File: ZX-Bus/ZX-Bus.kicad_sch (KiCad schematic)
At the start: 40 parts, among them J1 DIP-40 Pins, J2 Conn_01x04_Pin, J3 Conn_01x08_Pin, J4 Power, J5 Main board power, J6 12V, J7 5V, J8 Reset, U1 Z84C00xxP, U2 74LS245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

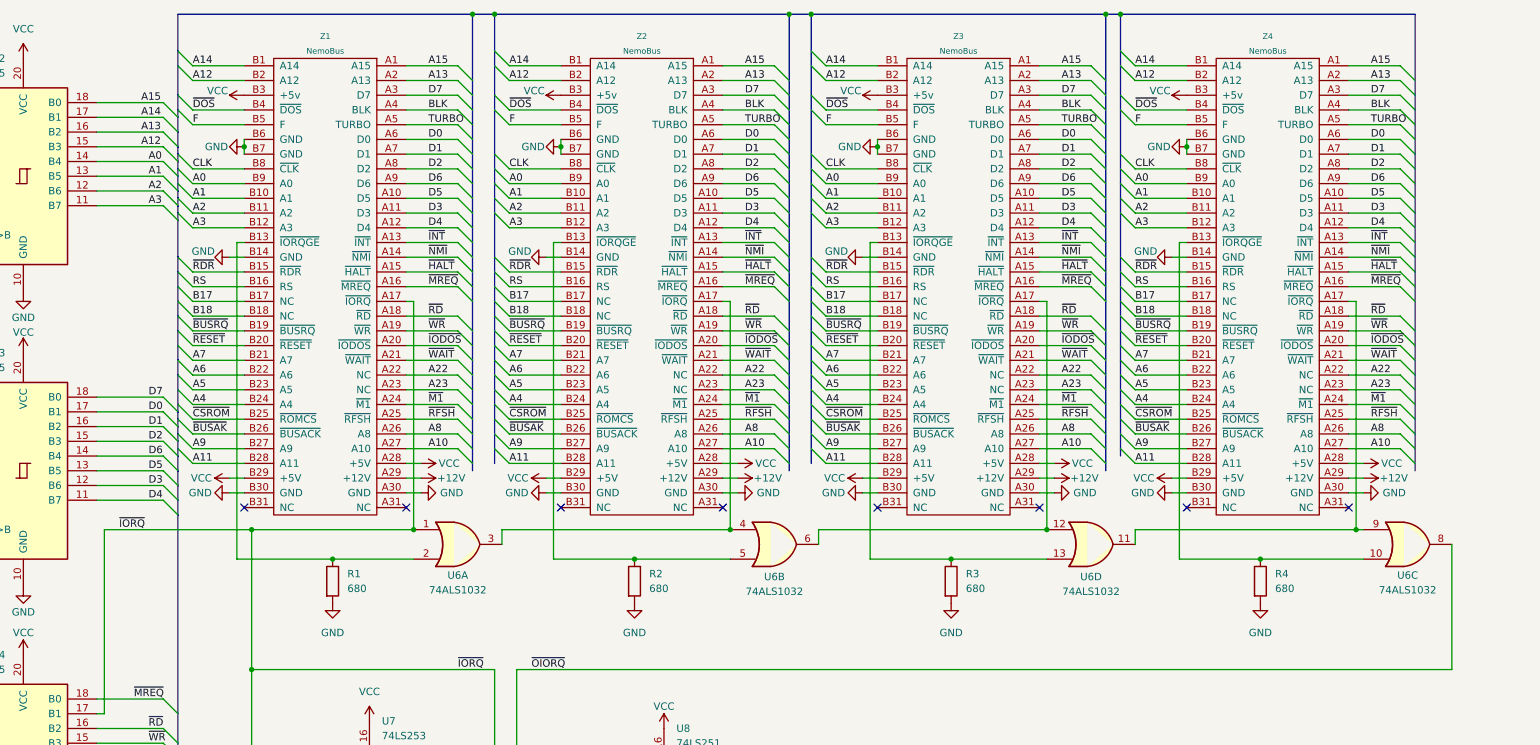
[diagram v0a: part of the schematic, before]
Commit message: ZX-Bus: Flip slots on the schematic
This is actually original orientation, during schematic creation i flipped them
for historical reason. It's easier to compare with other versions.
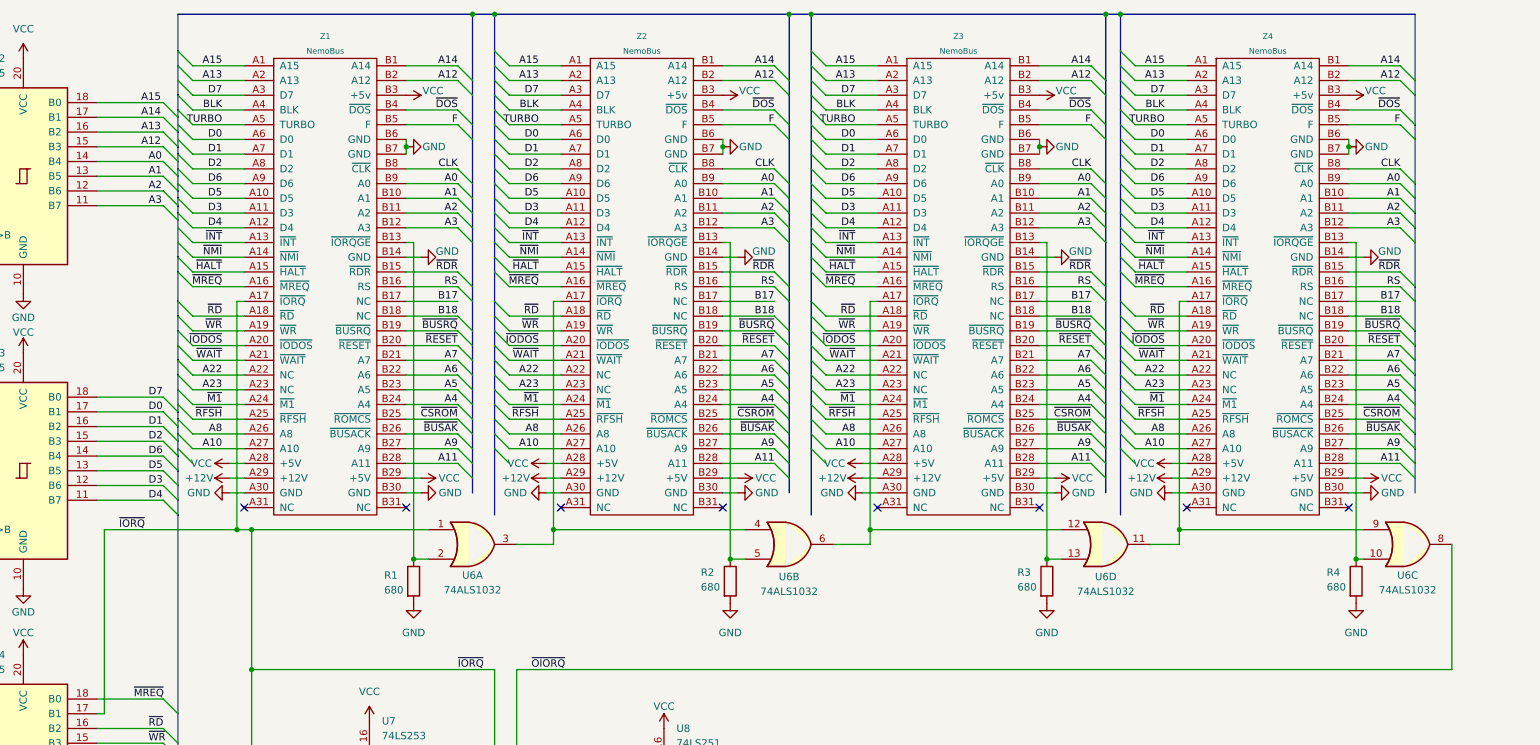
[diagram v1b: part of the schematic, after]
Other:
- moved on the sheet: R1, R2, R3, R4, U6A, U6B, U6D

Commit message: ZX-Bus: Complete v1
Add missing parts and complete layout
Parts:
- removed C12, C13: 220uF, Capacitor_THT:CP_Radial_D5.0mm_P2.50mm, symbol Device:C_Polarized
- removed J2: Conn_01x04_Pin, Connector_PinHeader_2.54mm:PinHeader_1x04_P2.54mm_Vertical, symbol Connector:Conn_01x04_Pin
- removed J3: Conn_01x08_Pin, Connector_PinHeader_2.54mm:PinHeader_1x08_P2.54mm_Vertical, symbol Connector:Conn_01x08_Pin
- added C12, C13, C14: 0.1uF, Capacitor_THT:C_Disc_D4.3mm_W1.9mm_P5.00mm, symbol Device:C
- added C15, C16: 220uF, Capacitor_THT:CP_Radial_D5.0mm_P2.50mm, symbol Device:C_Polarized
- added H3: MountingHole 3mm, MountingHole:MountingHole_3mm_Pad, symbol Mechanical:MountingHole_Pad
- added J2: PLS-3, Connector_PinHeader_2.54mm:PinHeader_1x03_P2.54mm_Vertical, symbol Connector:Conn_01x03_Pin
- added J3: PLS-6, Connector_PinHeader_2.54mm:PinHeader_1x05_P2.54mm_Vertical, symbol Connector:Conn_01x05_Pin
- added J9: PLS-2R, Connector_PinHeader_2.54mm:PinHeader_1x02_P2.54mm_Horizontal, symbol Connector:Conn_01x02_Pin
- added JP2: ROM type, Connector_PinHeader_2.54mm:PinHeader_1x03_P2.54mm_Vertical, symbol Jumper:Jumper_3_Bridged12
- added R5: 510, Resistor_THT:R_Axial_DIN0207_L6.3mm_D2.5mm_P10.16mm_Horizontal, symbol Device:R
- added R6: 10K, Resistor_THT:R_Axial_DIN0204_L3.6mm_D1.6mm_P2.54mm_Vertical, symbol Device:R
- added U10, U9: 27128, Package_DIP:DIP-28_W15.24mm_Socket, symbol Memory_EPROM:27128
- added U11: 74ALS1032, Package_DIP:DIP-14_W7.62mm, symbol 74xx:74LS32
- J8: footprint Connector_PinHeader_2.54mm:PinHeader_1x02_P2.54mm_Horizontal -> Connector_PinHeader_2.54mm:PinHeader_1x02_P2.54mm_Vertical
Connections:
- net *A0: now also U10.10 (A0), U9.10 (A0)
- net *A1: now also U10.9 (A1), U9.9 (A1)
- net *A10: now also U10.21 (A10), U9.21 (A10)
- net *A11: now also U10.23 (A11), U9.23 (A11)
- net *A12: now also U10.2 (A12), U9.2 (A12)
- net *A13: now also U10.26 (A13), U9.26 (A13)
- net *A14: now also U11.2
- net *A15: now also U11.1
- net *A2: now also U10.8 (A2), U9.8 (A2)
- net *A3: now also U10.7 (A3), U9.7 (A3)
- net *A4: now also U10.6 (A4), U9.6 (A4)
- net *A5: now also U10.5 (A5), U9.5 (A5)
- net *A6: now also U10.4 (A6), U9.4 (A6)
- net *A7: now also U10.3 (A7), U9.3 (A7)
- net *A8: now also U10.25 (A8), U9.25 (A8)
- net *A9: now also U10.24 (A9), U9.24 (A9)
- net *D0: now also U10.11 (D0), U9.11 (D0)
- net *D1: now also U10.12 (D1), U9.12 (D1)
- net *D2: now also U10.13 (D2), U9.13 (D2)
- net *D3: now also U10.15 (D3), U9.15 (D3)
- net *D4: now also U10.16 (D4), U9.16 (D4)
- net *D5: now also U10.17 (D5), U9.17 (D5)
- net *D6: now also U10.18 (D6), U9.18 (D6)
- net *D7: now also U10.19 (D7), U9.19 (D7)
- net *~{MREQ}: now also U11.4
- net *~{RD}: now also U11.5
- net +12V: now also C16.1
- net A22: now also J3.4 (Pin_4)
- net A23: now also J3.5 (Pin_5)
- net B17: now also J3.1 (Pin_1)
- net B18: now also J3.2 (Pin_2)
- net BLK: now also J2.1 (Pin_1)
- net F: now also J2.3 (Pin_3)
- net GND: now also C12.2, C13.2, C14.2, C15.2, C16.2, H3.1, U10.14 (GND), U11.12, U11.13, U11.7 (GND), U9.14 (GND)
- net RS: now also R6.1
- net TURBO: now also J2.2 (Pin_2)
- net VCC: now also C12.1, C13.1, C14.1, C15.1, JP2.1 (A), R6.2, U10.1 (VPP), U10.27 (~{PGM}), U10.28 (VCC), U11.14 (VCC), U9.1 (VPP), U9.28 (VCC)
- net ~{CSROM}: now also R5.2, U11.8
- net ~{DOS}: now also J9.1 (Pin_1), JP2.3 (B), U10.22 (~{OE})
- net ~{RDR}: now also R5.1, U10.20 (~{CE}), U9.20 (~{CE})
- net ~{IODOS} renamed A20
- net A20: now also J3.3 (Pin_3)
- new net: U11.10, U11.3
- new net: U11.6, U11.9
- new net: JP2.2 (C), U9.27 (~{PGM})
- new net DOS: J9.2 (Pin_2), U9.22 (~{OE})
- no-connect marks 15 -> 16
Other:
- title: (none) -> NemoBus for Pentagon-48
- moved on the sheet: C1, C10, C11, C2, C3, C4, C5, C6, C8, C9, H1, H2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

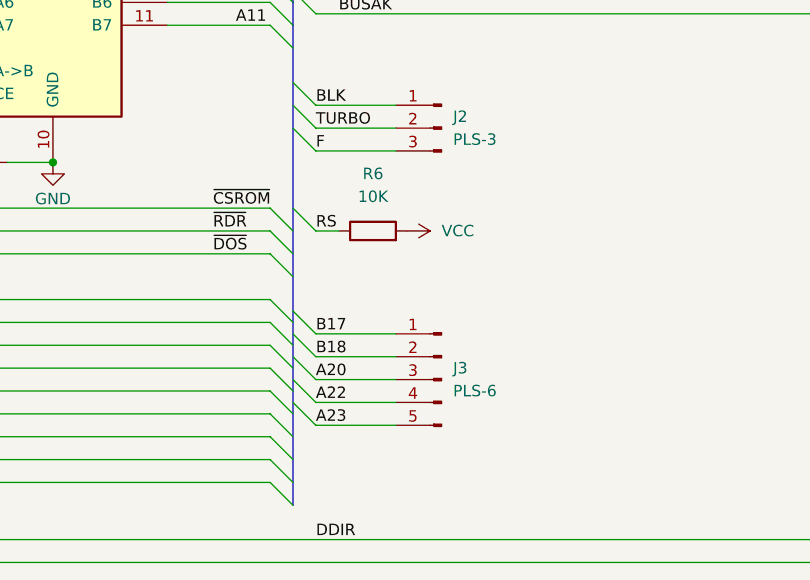
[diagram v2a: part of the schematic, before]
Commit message: ZX-Bus: Some corrections
Corrected size and layout after verification. SL-62 footprints with proper
courtyards.
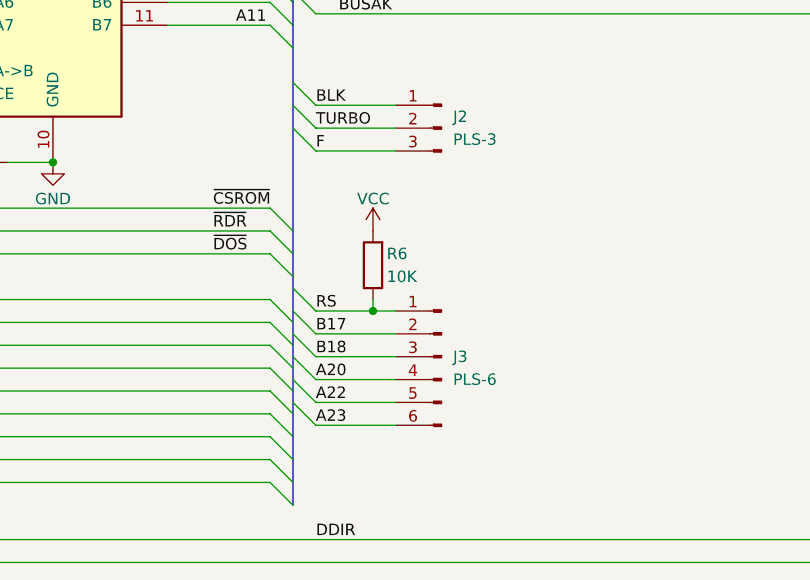
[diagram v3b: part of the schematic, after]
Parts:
- removed J3: PLS-6, Connector_PinHeader_2.54mm:PinHeader_1x05_P2.54mm_Vertical, symbol Connector:Conn_01x05_Pin
- added J3: PLS-6, Connector_PinHeader_2.54mm:PinHeader_1x06_P2.54mm_Vertical, symbol Connector:Conn_01x06_Pin
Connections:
- net A20: now also J3.4 (Pin_4)
- net A22: now also J3.5 (Pin_5)
- net A23: now also J3.6 (Pin_6)
- net B17: now also J3.2 (Pin_2)
- net B18: now also J3.3 (Pin_3)
- net RS: now also J3.1 (Pin_1)
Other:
- moved on the sheet: R6
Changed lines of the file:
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@@
 	)
 	(junction
+		(at 189.23 254)
+		(diameter 0)
+		(color 0 0 0 0)
+	)
+	(junction
 		(at 353.06 124.46)
 		(diameter 0)
@@
 	)
 	(bus_entry
+		(at 180.34 251.46)
+		(size 2.54 2.54)
+		(stroke
+			(width 0)
+			(type default)
+		)
+	)
+	(bus_entry
 		(at 234.95 105.41)
 		(size 2.54 2.54)
@@
 	)
 	(bus_entry
-		(at 180.34 242.57)
-		(size 2.54 2.54)
-		(stroke
-			(width 0)
-			(type default)
-		)
-	)
-	(bus_entry
 		(at 177.8 255.27)
 		(size 2.54 2.54)
@@
 	(wire
 		(pts
-			(xy 182.88 245.11) (xy 185.42 245.11)
-		)
-		(stroke
-			(width 0)
-			(type default)
-		)
-	)
-	(wire
-		(pts
 			(xy 166.37 58.42) (xy 177.8 58.42)
 		)
@@
 		)
 	)
+	(wire
+		(pts
+			(xy 189.23 254) (xy 189.23 252.73)
+		)
+		(stroke
+			(width 0)
+			(type default)
+		)
+	)
 	(bus
 		(pts
@@
 	(wire
 		(pts
+			(xy 182.88 254) (xy 189.23 254)
+		)
+		(stroke
+			(width 0)
+			(type default)
+		)
+	)
+	(wire
+		(pts
 			(xy 85.09 110.49) (xy 93.98 110.49)
 		)
@@
 		)
 	)
+	(wire
+		(pts
+			(xy 189.23 254) (xy 191.77 254)
+		)
+		(stroke
+			(width 0)
+			(type default)
+		)
+	)
 	(bus
 		(pts
@@
 		)
 	)
+	(label "RS"
+		(at 182.88 254 0)
+		(effects
+			(font
+				(size 1.27 1.27)
+			)
+			(justify left bottom)
+		)
+	)
 	(label "*A8"
 		(at 129.54 214.63 0)
@@
 		)
 	)
-	(label "RS"
-		(at 182.88 245.11 0)
-		(effects
-			(font
-				(size 1.27 1.27)
-			)
-			(justify left bottom)
-		)
-	)
 	(label "*D7"
 		(at 129.54 101.6 0)
@@
 	)
 	(symbol
-		(lib_id "Connector:Conn_01x05_Pin")
-		(at 196.85 261.62 0)
-		(mirror y)
-		(unit 1)
-		(body_style 1)
-		(exclude_from_sim no)
-		(in_bom yes)
-		(on_board yes)
-		(in_pos_files yes)
-		(dnp no)
-		(fields_autoplaced yes)
-		(property "Reference" "J3"
-			(at 198.12 260.3499 0)
-			(show_name no)
-			(do_not_autoplace no)
-			(effects
-				(font
-					(size 1.27 1.27)
-				)
-				(justify right)
-			)
-		)
-		(property "Value" "PLS-6"
-			(at 198.12 262.8899 0)
-			(show_name no)
-			(do_not_autoplace no)
-			(effects
-				(font
-					(size 1.27 1.27)
-				)
-				(justify right)
-			)
-		)
-		(property "Footprint" "Connector_PinHeader_2.54mm:PinHeader_1x05_P2.54mm_Vertical"
-			(at 196.85 261.62 0)
-			(hide yes)
-			(show_name no)
-			(do_not_autoplace no)
-			(effects
-				(font
-					(size 1.27 1.27)
-				)
-			)
-		)
-		(property "Datasheet" ""
-			(at 196.85 261.62 0)
-			(hide yes)
-			(show_name no)
-			(do_not_autoplace no)
-			(effects
-				(font
-					(size 1.27 1.27)
-				)
-			)
-		)
-		(property "Description" "Generic connector, single row, 01x05, script generated"
-			(at 196.85 261.62 0)
-			(hide yes)
-			(show_name no)
-			(do_not_autoplace no)
-			(effects
-				(font
-					(size 1.27 1.27)
-				)
-			)
-		)
-		(pin "4"
-		)
-		(pin "1"
-		)
-		(pin "3"
-		)
-		(pin "2"
-		)
-		(pin "5"
-		)
-		(instances
-			(project "ZX-Bus"
-				(path "/e919f151-b328-4d2c-bb3c-73ab87d30906"
-					(reference "J3")
-					(unit 1)
-				)
-			)
-		)
-	)
-	(symbol
 		(lib_id "power:VCC")
 		(at 331.47 115.57 270)
@@
 	(symbol
 		(lib_id "power:VCC")
-		(at 193.04 245.11 270)
+		(at 189.23 245.11 0)
 		(unit 1)
 		(body_style 1)
@@
 		(in_pos_files yes)
 		(dnp no)
-		(fields_autoplaced yes)
 		(property "Reference" "#PWR087"
-			(at 189.23 245.11 0)
+			(at 189.23 248.92 0)
 			(hide yes)
 			(show_name no)
@@
 		)
 		(property "Value" "VCC"
-			(at 196.85 245.1099 90)
+			(at 187.452 241.554 0)
 			(show_name no)
 			(do_not_autoplace no)
@@
 		)
 		(property "Footprint" ""
-			(at 193.04 245.11 0)
+			(at 189.23 245.11 0)
 			(hide yes)
 			(show_name no)
@@
 		)
 		(property "Datasheet" ""
-			(at 193.04 245.11 0)
+			(at 189.23 245.11 0)
 			(hide yes)
 			(show_name no)
@@
 		)
 		(property "Description" "Power symbol creates a global label with name \"VCC\""
-			(at 193.04 245.11 0)
+			(at 189.23 245.11 0)
 			(hide yes)
 			(show_name no)
@@
 	(symbol
 		(lib_id "Device:R")
-		(at 189.23 245.11 90)
+		(at 189.23 248.92 180)
 		(unit 1)
 		(body_style 1)
@@
 		(in_pos_files yes)
 		(dnp no)
-		(fields_autoplaced yes)
 		(property "Reference" "R6"
-			(at 189.23 238.76 90)
+			(at 190.754 247.65 0)
 			(show_name no)
 			(do_not_autoplace no)
@@
 					(size 1.27 1.27)
 				)
+				(justify right)
 			)
 		)
 		(property "Value" "10K"
-			(at 189.23 241.3 90)
+			(at 190.754 250.19 0)
 			(show_name no)
 			(do_not_autoplace no)
@@
 					(size 1.27 1.27)
 				)
+				(justify right)
 			)
 		)
 		(property "Footprint" "Resistor_THT:R_Axial_DIN0204_L3.6mm_D1.6mm_P2.54mm_Vertical"
-			(at 189.23 246.888 90)
+			(at 191.008 248.92 90)
 			(hide yes)
 			(show_name no)
@@
 		)
 		(property "Datasheet" ""
-			(at 189.23 245.11 0)
+			(at 189.23 248.92 0)
 			(hide yes)
 			(show_name no)
@@
 		)
 		(property "Description" "Resistor"
-			(at 189.23 245.11 0)
+			(at 189.23 248.92 0)
 			(hide yes)
 			(show_name no)
@@
 					(unit 1)
 				)
+			)
+		)
+	)
+	(symbol
+		(lib_id "Connector:Conn_01x06_Pin")
+		(at 196.85 259.08 0)
+		(mirror y)
+		(unit 1)
+		(body_style 1)
+		(exclude_from_sim no)
+		(in_bom yes)
+		(on_board yes)
+		(in_pos_files yes)
+		(dnp no)
+		(fields_autoplaced yes)
+		(property "Reference" "J3"
+			(at 198.12 259.0799 0)
+			(show_name no)
+			(do_not_autoplace no)
+			(effects
+				(font
+					(size 1.27 1.27)
+				)
+				(justify right)
+			)
+		)
+		(property "Value" "PLS-6"
+			(at 198.12 261.6199 0)
+			(show_name no)
+			(do_not_autoplace no)
+			(effects
+				(font
+					(size 1.27 1.27)
+				)
+				(justify right)
+			)
+		)
+		(property "Footprint" "Connector_PinHeader_2.54mm:PinHeader_1x06_P2.54mm_Vertical"
+			(at 196.85 259.08 0)
+			(hide yes)
+			(show_name no)
+			(do_not_autoplace no)
+			(effects
+				(font
+					(size 1.27 1.27)
+				)
+			)
+		)
+		(property "Datasheet" ""
+			(at 196.85 259.08 0)
+			(hide yes)
+			(show_name no)
+			(do_not_autoplace no)
+			(effects
+				(font
+					(size 1.27 1.27)
+				)
+			)
+		)
+		(property "Description" "Generic connector, single row, 01x06, script generated"
+			(at 196.85 259.08 0)
+			(hide yes)
+			(show_name no)
+			(do_not_autoplace no)
+			(effects
+				(font
+					(size 1.27 1.27)
+				)
+			)
+		)
+		(pin "3"
+		)
+		(pin "1"
+		)
+		(pin "2"
+		)
+		(pin "6"
+		)
+		(pin "5"
+		)
+		(pin "4"
+		)
+		(instances
+			(project "ZX-Bus"
+				(path "/e919f151-b328-4d2c-bb3c-73ab87d30906"
+					(reference "J3")
+					(unit 1)
+				)

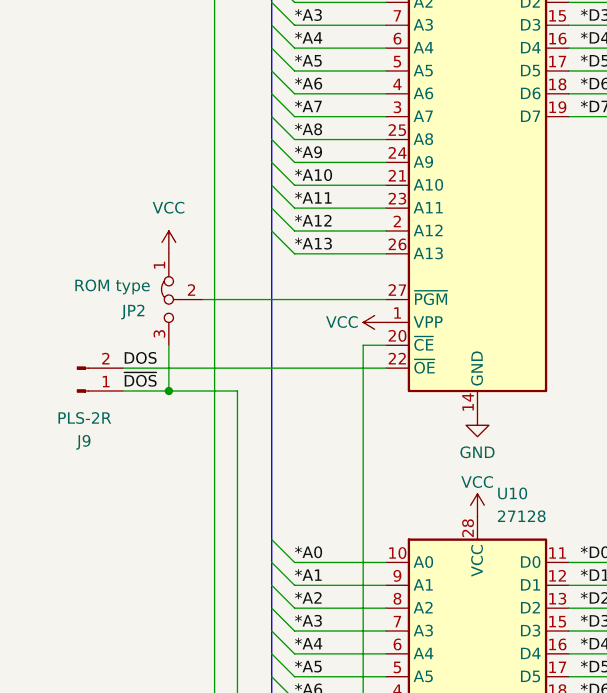
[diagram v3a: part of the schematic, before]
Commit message: ZX-Bus: Fix ROM type select jumper
We actually need to switch two lines.
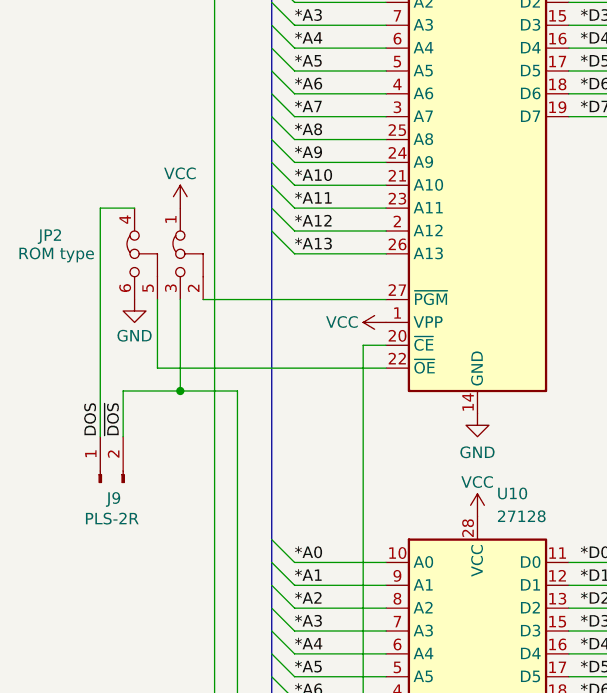
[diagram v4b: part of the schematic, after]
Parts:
- JP2: footprint Connector_PinHeader_2.54mm:PinHeader_1x03_P2.54mm_Vertical -> Connector_PinHeader_2.54mm:PinHeader_3x02_P2.54mm_Vertical
- R6: footprint Resistor_THT:R_Axial_DIN0204_L3.6mm_D1.6mm_P2.54mm_Vertical -> Resistor_THT:R_Axial_DIN0207_L6.3mm_D2.5mm_P10.16mm_Horizontal
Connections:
- net DOS: now also J9.1 (Pin_1), JP2.4 (A); no longer J9.2 (Pin_2), U9.22 (~{OE})
- net GND: now also JP2.6 (B)
- net ~{DOS}: now also J9.2 (Pin_2); no longer J9.1 (Pin_1)
- new net: JP2.5 (C), U9.22 (~{OE})

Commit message: ZX-Bus: More taps
Add 14MHz tap to U2 (on main board). Add some more power headers so that we are
able to connect the board with no need to solder more power cables. It's
possible to drill the main board in those places and install power pins.
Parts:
- added J10: DIP14, DIP-14_W7.62mm-Pins, symbol Connector_Generic:Conn_02x07_Counter_Clockwise
- added J11: PBS-4, Connector_PinSocket_2.54mm:PinSocket_1x04_P2.54mm_Vertical, symbol Connector:Conn_01x04_Socket
- added J12: PBS-5, Connector_PinSocket_2.54mm:PinSocket_1x05_P2.54mm_Vertical, symbol Connector:Conn_01x05_Socket
- added JP3: 14 MHz phase, Connector_PinHeader_2.54mm:PinHeader_1x03_P2.54mm_Vertical, symbol Jumper:Jumper_3_Bridged12
- added U12: 74LS04, Package_DIP:DIP-14_W7.62mm_Socket, symbol 74xx:74LS04
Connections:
- net F: now also JP3.2 (C)
- net GND: now also J10.7 (Pin_7), J12.1 (Pin_1), J12.2 (Pin_2), J12.3 (Pin_3), J12.4 (Pin_4), J12.5 (Pin_5), U12.7 (GND)
- net VCC: now also J10.14 (Pin_14), J11.1 (Pin_1), J11.2 (Pin_2), J11.3 (Pin_3), J11.4 (Pin_4), U12.14 (VCC)
- new net: J10.5 (Pin_5), U12.5
- new net: J10.6 (Pin_6), U12.6
- new net: J10.1 (Pin_1), U12.1
- new net: J10.2 (Pin_2), U12.2
- new net: J10.12 (Pin_12), U12.12
- new net: J10.13 (Pin_13), U12.13
- new net: J10.3 (Pin_3), U12.3
- new net: J10.4 (Pin_4), U12.4
- new net: J10.10 (Pin_10), U12.10
- new net: J10.11 (Pin_11), U12.11
- new net: J10.8 (Pin_8), JP3.1 (A), U12.8
- new net: J10.9 (Pin_9), JP3.3 (B), U12.9
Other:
- moved on the sheet: C15, C16, J4, J5, J6, J7, U11E, U6E
